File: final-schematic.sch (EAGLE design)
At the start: 31 parts, among them T1 2N2222, U1 STM32F042K6, U2 IP4220CZ6, U3 MCP1802T-3302I/OT

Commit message: actually final schematic
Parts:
- removed JP4: (no value), pinhead:PINHD-1X2
- added JP5: (no value), jumper:JP1E
- added TP1, TP2, TP3, TP4, TP5, TP6, TP7: TPB2,54, testpad:TPB2,54
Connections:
- new net BUZ: R10.1, TP7.TP, U1.PA2
- net +5V: now also JP5.2; no longer JP4.1
- net BUT1: now also TP3.TP
- net BUT2: now also TP4.TP
- net N$1: now also TP5.TP
- net N$2: now also TP6.TP
- net N$3: now also TP1.TP
- net N$4: now also TP2.TP
- net VBUS: now also JP5.1; no longer JP4.2
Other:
- note removed: "Clock goes in here >"
- note removed: "FOURIC: Add switch here"
- note removed: "FOURIC: Change these to supply symbols"
- moved on the sheet: C4, C5, C6, C7, C8, CN1, D1, D2, D3, JP1, JP2, JP3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

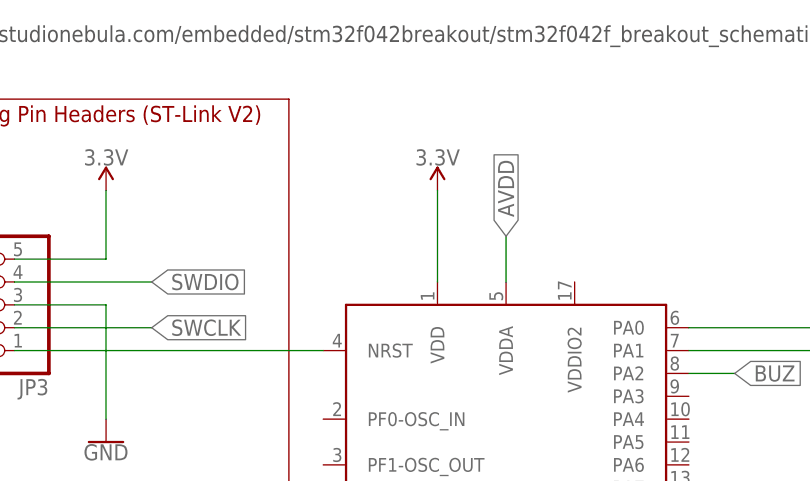
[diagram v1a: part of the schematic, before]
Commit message: add bypass capacitor to power supply of MCU
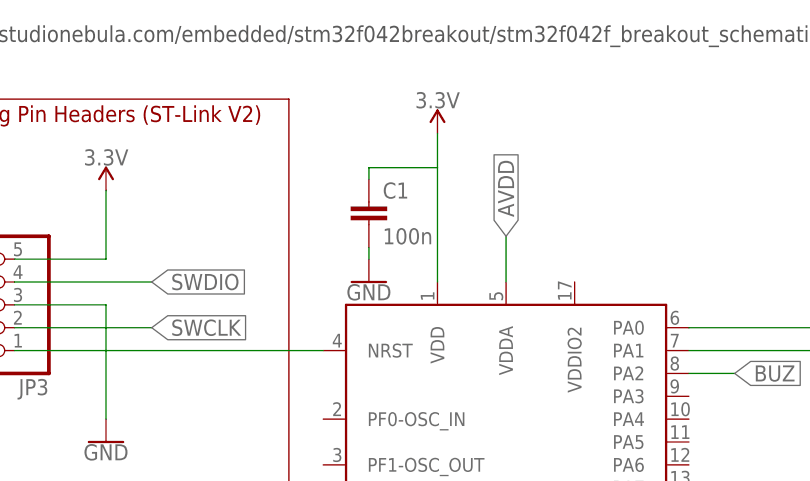
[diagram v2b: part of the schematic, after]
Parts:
- added C1: 100n, rcl:C-EUC0805
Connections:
- new net N$11: C1.2
- net 3.3V: now also C1.1
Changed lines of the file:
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@@
 <?xml version="1.0" encoding="utf-8"?>
 <!DOCTYPE eagle SYSTEM "eagle.dtd">
-<eagle version="8.4.0">
+<eagle version="8.4.1">
 <drawing>
 <settings>
@@
 <setting verticaltext="up"/>
 </settings>
-<grid distance="0.05" unitdist="inch" unit="inch" style="lines" multiple="2" display="no" altdistance="0.01" altunitdist="inch" altunit="inch"/>
+<grid distance="0.05" unitdist="inch" unit="inch" style="lines" multiple="2" display="yes" altdistance="0.01" altunitdist="inch" altunit="inch"/>
 <layers>
 <layer number="1" name="Top" color="4" fill="1" visible="no" active="no"/>
@@
 <part name="TP6" library="testpad" library_urn="urn:adsk.eagle:library:385" deviceset="TP" device="B2,54" package3d_urn="urn:adsk.eagle:package:27948/1"/>
 <part name="TP7" library="testpad" library_urn="urn:adsk.eagle:library:385" deviceset="TP" device="B2,54" package3d_urn="urn:adsk.eagle:package:27948/1"/>
+<part name="C1" library="rcl" library_urn="urn:adsk.eagle:library:334" deviceset="C-EU" device="C0805" package3d_urn="urn:adsk.eagle:package:23617/2" value="100n"/>
+<part name="GND11" library="SparkFun-PowerSymbols" library_urn="urn:adsk.eagle:library:530" deviceset="GND" device=""/>
 </parts>
 <sheets>
@@
 <instances>
 <instance part="U1" gate="G$1" x="0" y="0"/>
-<instance part="SUPPLY3" gate="G$1" x="-7.62" y="35.56"/>
+<instance part="SUPPLY3" gate="G$1" x="-7.62" y="41.91"/>
 <instance part="GND3" gate="1" x="0" y="-35.56"/>
 <instance part="JP3" gate="A" x="-57.15" y="22.86" rot="R180"/>
@@
 <instance part="TP6" gate="G$1" x="38.1" y="15.24" rot="R180"/>
 <instance part="TP7" gate="G$1" x="-111.76" y="13.97"/>
+<instance part="C1" gate="G$1" x="-15.24" y="34.29"/>
+<instance part="GND11" gate="1" x="-15.24" y="25.4"/>
 </instances>
 <busses>
@@
 <pinref part="U1" gate="G$1" pin="VDD"/>
 <pinref part="SUPPLY3" gate="G$1" pin="3.3V"/>
-<wire x1="-7.62" y1="25.4" x2="-7.62" y2="35.56" width="0.1524" layer="91"/>
+<wire x1="-7.62" y1="25.4" x2="-7.62" y2="38.1" width="0.1524" layer="91"/>
+<pinref part="C1" gate="G$1" pin="1"/>
+<wire x1="-7.62" y1="38.1" x2="-7.62" y2="41.91" width="0.1524" layer="91"/>
+<wire x1="-15.24" y1="36.83" x2="-15.24" y2="38.1" width="0.1524" layer="91"/>
+<wire x1="-15.24" y1="38.1" x2="-7.62" y2="38.1" width="0.1524" layer="91"/>
 </segment>
 <segment>
@@
 </segment>
 </net>
+<net name="N$11" class="0">
+<segment>
+<pinref part="C1" gate="G$1" pin="2"/>
+<wire x1="-15.24" y1="29.21" x2="-15.24" y2="27.94" width="0.1524" layer="91"/>
+<pinref part="GND11" gate="1" pin="GND"/>
+</segment>
+</net>
